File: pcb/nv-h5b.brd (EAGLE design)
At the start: 8 x 20 mm, 17 parts, among them IC1 TINY13A-20SSU, J1 22-05-7038-03

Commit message: PCB: add version.
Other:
- board text added: "v1.0"
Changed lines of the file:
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@@
 <grid distance="1.27" unitdist="mm" unit="mm" style="dots" multiple="2" display="no" altdistance="0.3175" altunitdist="mm" altunit="mm"/>
 <layers>
-<layer number="1" name="Top" color="3" fill="1" visible="yes" active="yes"/>
+<layer number="1" name="Top" color="3" fill="1" visible="no" active="yes"/>
 <layer number="2" name="Route2" color="16" fill="1" visible="no" active="no"/>
 <layer number="3" name="Route3" color="17" fill="1" visible="no" active="no"/>
@@
 <layer number="14" name="Route14" color="22" fill="1" visible="no" active="no"/>
 <layer number="15" name="Route15" color="23" fill="1" visible="no" active="no"/>
-<layer number="16" name="Bottom" color="4" fill="1" visible="no" active="yes"/>
+<layer number="16" name="Bottom" color="4" fill="1" visible="yes" active="yes"/>
 <layer number="17" name="Pads" color="2" fill="1" visible="yes" active="yes"/>
 <layer number="18" name="Vias" color="2" fill="1" visible="yes" active="yes"/>
 <layer number="19" name="Unrouted" color="6" fill="1" visible="yes" active="yes"/>
 <layer number="20" name="Dimension" color="24" fill="1" visible="yes" active="yes"/>
-<layer number="21" name="tPlace" color="7" fill="1" visible="yes" active="yes"/>
-<layer number="22" name="bPlace" color="7" fill="1" visible="no" active="yes"/>
-<layer number="23" name="tOrigins" color="15" fill="1" visible="yes" active="yes"/>
-<layer number="24" name="bOrigins" color="15" fill="1" visible="no" active="yes"/>
-<layer number="25" name="tNames" color="7" fill="1" visible="yes" active="yes"/>
-<layer number="26" name="bNames" color="7" fill="1" visible="no" active="yes"/>
+<layer number="21" name="tPlace" color="7" fill="1" visible="no" active="yes"/>
+<layer number="22" name="bPlace" color="7" fill="1" visible="yes" active="yes"/>
+<layer number="23" name="tOrigins" color="15" fill="1" visible="no" active="yes"/>
+<layer number="24" name="bOrigins" color="15" fill="1" visible="yes" active="yes"/>
+<layer number="25" name="tNames" color="7" fill="1" visible="no" active="yes"/>
+<layer number="26" name="bNames" color="7" fill="1" visible="yes" active="yes"/>
 <layer number="27" name="tValues" color="7" fill="1" visible="no" active="yes"/>
 <layer number="28" name="bValues" color="7" fill="1" visible="no" active="yes"/>
@@
 <layer number="48" name="Document" color="7" fill="1" visible="no" active="yes"/>
 <layer number="49" name="Reference" color="7" fill="1" visible="no" active="yes"/>
-<layer number="51" name="tDocu" color="7" fill="1" visible="yes" active="yes"/>
-<layer number="52" name="bDocu" color="7" fill="1" visible="no" active="yes"/>
+<layer number="51" name="tDocu" color="7" fill="1" visible="no" active="yes"/>
+<layer number="52" name="bDocu" color="7" fill="1" visible="yes" active="yes"/>
 <layer number="88" name="SimResults" color="9" fill="1" visible="no" active="no"/>
 <layer number="89" name="SimProbes" color="9" fill="1" visible="no" active="no"/>
@@
 <layer number="98" name="Guide" color="6" fill="1" visible="no" active="no"/>
 <layer number="99" name="SpiceOrder" color="5" fill="1" visible="no" active="no"/>
+<layer number="116" name="centerDrill" color="7" fill="1" visible="yes" active="yes"/>
 </layers>
 <board>
@@
 <text x="2.2225" y="5.08" size="1.6764" layer="26" rot="MR0">+</text>
 <text x="4.1275" y="2.8575" size="0.8128" layer="26" font="vector" rot="MR0" align="bottom-center">NV-H5B</text>
+<text x="4.1275" y="4.1275" size="0.8128" layer="26" font="vector" rot="MR0" align="bottom-center">v1.0</text>
 </plain>
 <attributes>

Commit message: sch: use ATtiny25.
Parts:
- IC1: value TINY13A-20SSU -> ATTINY25-20SU
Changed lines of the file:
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@@
 <attribute name="VALUE" x="2.8575" y="5.08" size="0.8128" layer="27" rot="R180"/>
 </element>
-<element name="IC1" library="atmel" library_urn="urn:adsk.eagle:library:105" package="8S1" package3d_urn="urn:adsk.eagle:package:4358/1" value="TINY13A-20SSU" x="5.08" y="12.7" smashed="yes" rot="R180">
+<element name="IC1" library="atmel" library_urn="urn:adsk.eagle:library:105" package="8S1" package3d_urn="urn:adsk.eagle:package:4358/1" value="ATTINY25-20SU" x="5.08" y="12.7" smashed="yes" rot="R180">
 <attribute name="MF" value="" x="-22.86" y="16.51" size="1.778" layer="27" rot="R180" display="off"/>
 <attribute name="MPN" value="ATTINY13-20SSU" x="-22.86" y="16.51" size="1.778" layer="27" rot="R180" display="off"/>

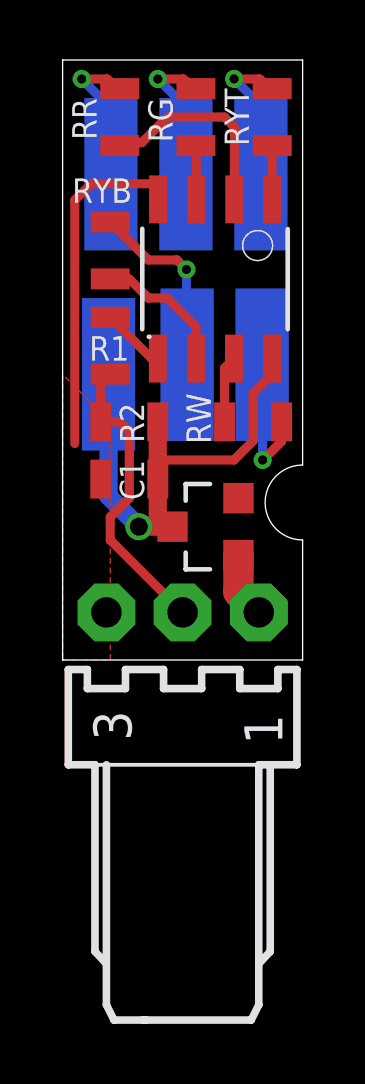
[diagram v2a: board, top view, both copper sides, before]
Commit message: Opravit orientaci vstupniho konektoru.
Bylo opacne GND & VCC.
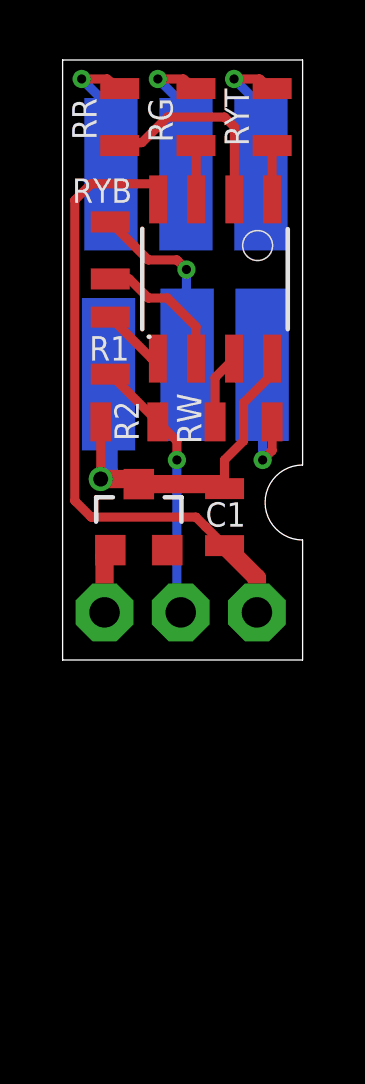
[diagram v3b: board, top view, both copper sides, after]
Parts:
- moved C1 3.42 mm to (5.40, 4.76), turned to 270 degrees
- moved D2 2.25 mm to (2.54, 4.76), turned to 0 degrees
- moved RW 0.32 mm to (6.03, 7.94)
- moved J1 0.06 mm to (3.94, 1.59), flipped to the bottom
- turned R2 to 0 degrees
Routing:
- net GND: track 11.6 -> 21.8 mm
- net VCC: track 16.9 -> 14.8 mm
- net DATAIN: track 10.2 -> 8.91 mm, vias 0 -> 1
- net YEL-BOT: track 6.98 -> 6.38 mm
- removed copper zone on layer 1, net GND
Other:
- board text added: "v2.0"
- board text removed: "v1.0"
